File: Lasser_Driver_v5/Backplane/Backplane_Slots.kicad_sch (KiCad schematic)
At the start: 24 parts, among them J1 294711-E, J2 294711-E, J3 294711-E, J4 294711-E, J5 294711-E, J6 294711-E, J7 294711-E, J8 294711-E

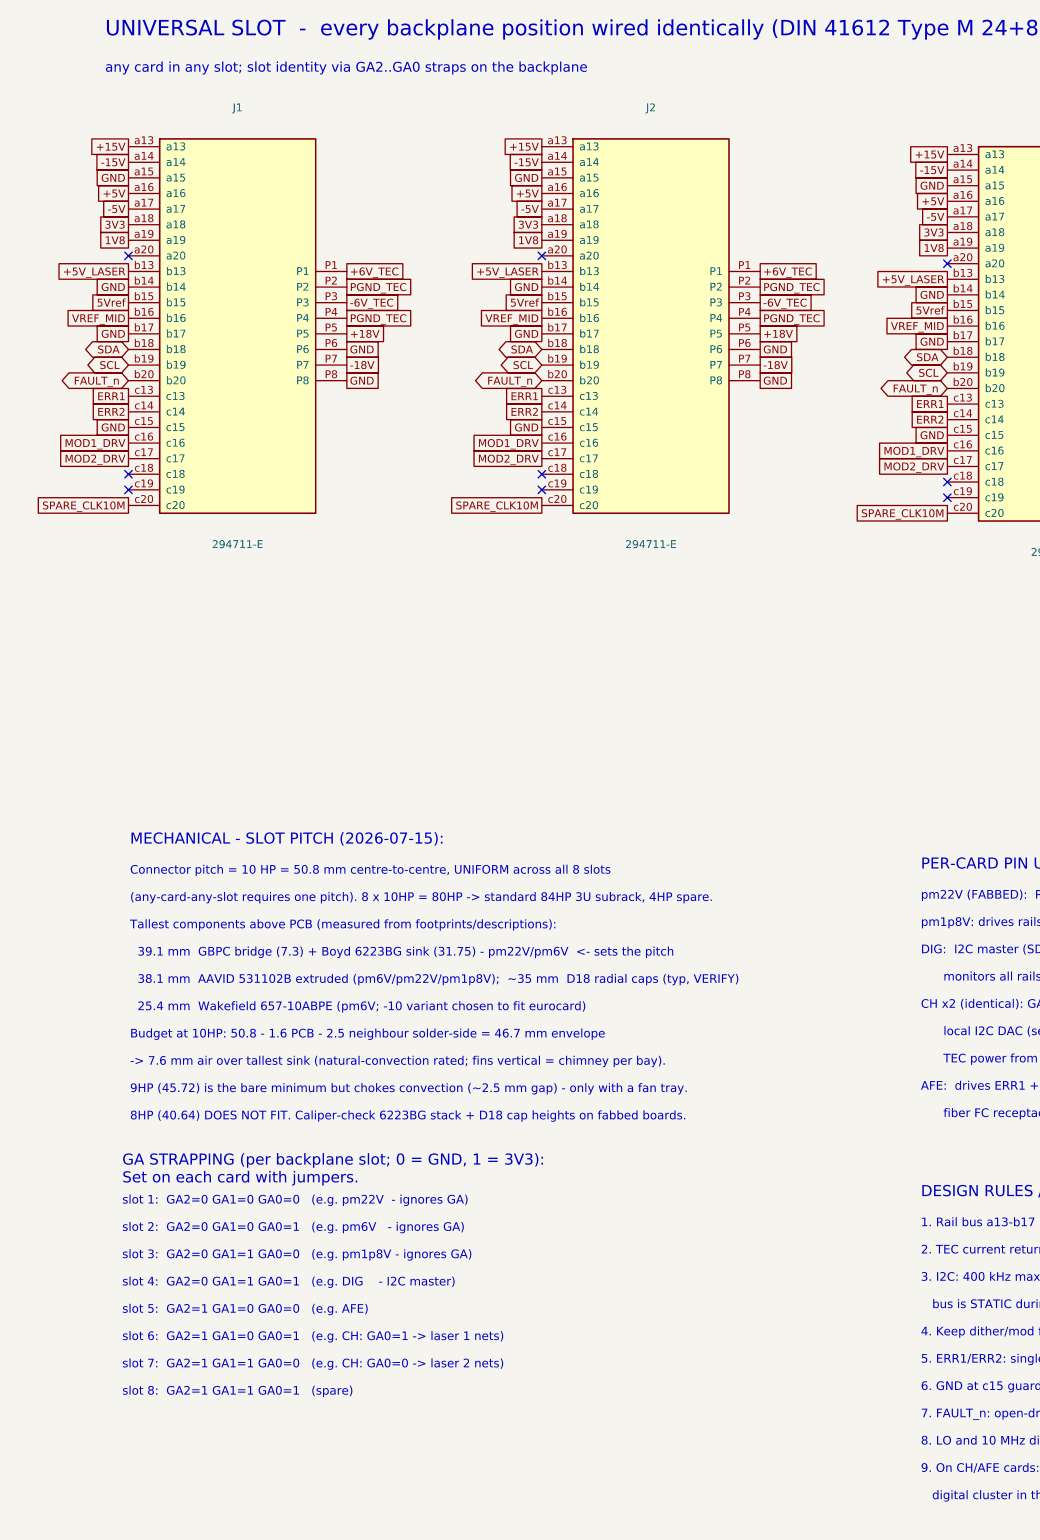
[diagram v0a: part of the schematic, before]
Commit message: Changed CH card to 6 layer. Added single pt grnd.
CH card is now layed out cleanly with 6 layers.
Added a single point connection with surge protection to the backplane.
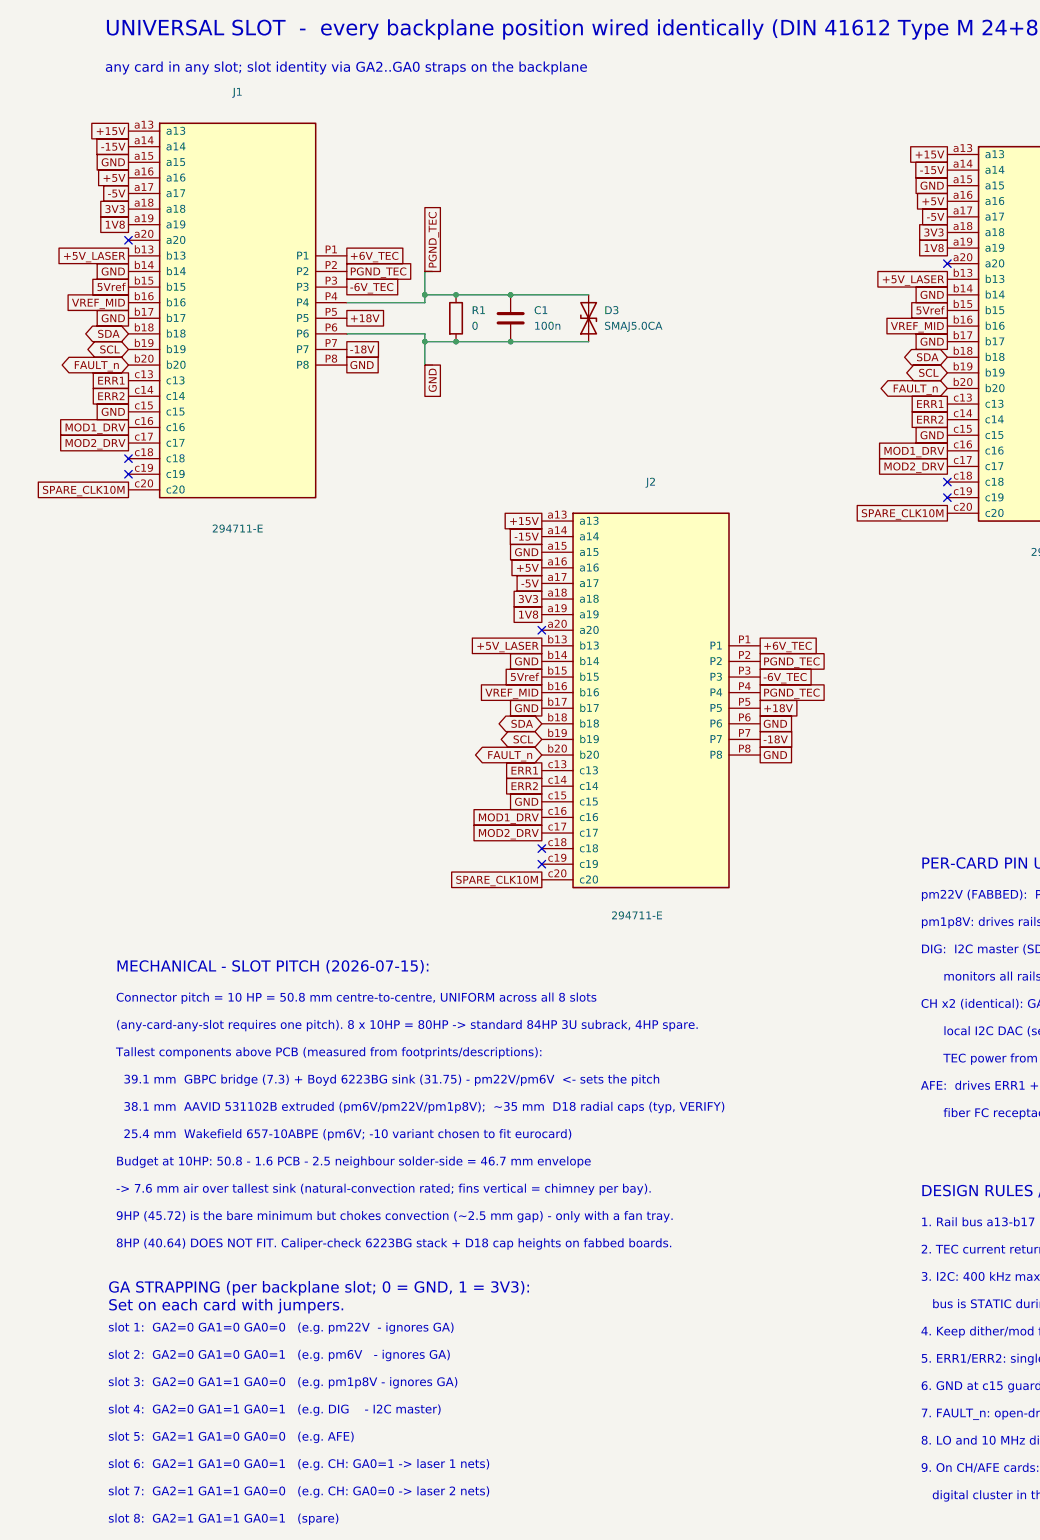
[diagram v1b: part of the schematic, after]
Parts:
- added C1: 100n, Capacitor_SMD:C_0805_2012Metric_Pad1.18x1.45mm_HandSolder, symbol Device:C
- added D3: SMAJ5.0CA, Diode_SMD:D_SMA-SMB_Universal_Handsoldering, symbol Device:D_TVS
- added R1: 0, Resistor_SMD:R_0805_2012Metric_Pad1.20x1.40mm_HandSolder, symbol Device:R
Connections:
- net GND: now also C1.2, D3.1 (A1), R1.2
- net PGND_TEC: now also C1.1, D3.2 (A2), R1.1
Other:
- moved on the sheet: J1, J2
